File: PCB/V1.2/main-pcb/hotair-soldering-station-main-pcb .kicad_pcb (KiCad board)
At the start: 2 copper layers, 100 x 70 mm, 146 parts, among them J1 230VAC_IN, J10 T12_power (NS-25 r2,54), J11 LCD_CON2 (JST r.2.0), J12 LCD_CON1 (JST r.2.0), J13 ICP (goldpin r2,54), J14 Unused_GPIO, J2 FRONT_PANEL (IDC r. 2,54), J3 EARTH_GND, J4 24V_IN (NS-25 r2,54), J5 PSUPPLY (PWZ-02S r.3,96), J6 HOTAIR_FAN (JST r,2,54), J7 HOTAIR_MEAS (JST r.2,5), J8 HOTAIR_HEATER (PWZ-02S r.3,96), J9 WEP (r.2,54), Q1 BC817, Q10 RFP15P05, Q11 BC817, Q12 BC817, Q13 BC817, Q14 BC807, Q15 RFP15P05, Q2 BC807, Q3 BC817, Q4 RFP15P05, Q5 BC817, Q6 BT139-600, Q7 BC817, Q8 BC807, Q9 BC817, U1 MOC3041M, U2 MAX31855KASA, U3 MP1584-Step-Down, U4 AP1117-ADJ, U5 LM741, U6 AD8606, U8 STM32F103C6Tx

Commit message: Silkscreen progress
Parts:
- U3: value MP1584-Step-Down -> MP1584
- moved R9 2.41 mm to (72.0, 40.9)
- moved G*** 1.59 mm to (77.9, 45.3)
- moved D12 0.43 mm to (109.0, 48.6)
- moved C16 0.38 mm to (67.8, 46.6)
- moved C19 0.13 mm to (75.8, 67.3)
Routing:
- net THERM_GND: track 31.0 -> 33.2 mm
- net IRON_T12_TEMP_ADC: track 55.4 -> 53.3 mm
- net UART_DBG_TX: track 26.3 -> 25.3 mm
- net +3V3: track 214.1 -> 214.8 mm

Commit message: Front panel rocker switch connector change, preparing pcb for production
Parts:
- C13, C18, C19, C20, C6, C8: footprint Capacitors:0603 -> Capacitors:0805
- C9: footprint Capacitor_SMD:C_0603_1608Metric -> Capacitors:0805
- U3: value MP1584 -> MP1584-Step-Down
- moved C19 0.51 mm to (75.9, 67.8)
- moved C9 0.30 mm to (75.9, 66.1)
- moved C8 0.18 mm to (77.9, 54.8)
- moved C18 0.15 mm to (87.0, 56.5)
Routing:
- net +3V3: track 214.8 -> 215.6 mm

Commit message: Front panel done
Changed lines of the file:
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@@
       (effects (font (size 1 1) (thickness 0.15)) (justify mirror))
     )
+    (fp_line (start -2.5 2) (end 7.66 2) (layer "B.SilkS") (width 0.12))
     (fp_line (start 0.69 3.27) (end 0.7 2) (layer "B.SilkS") (width 0.12))
-    (fp_line (start -2.58 3.27) (end -2.58 -2.1) (layer "B.SilkS") (width 0.12))
-    (fp_line (start -2.58 3.27) (end 7.66 3.27) (layer "B.SilkS") (width 0.12))
     (fp_line (start -2.58 -2.1) (end 7.66 -2.1) (layer "B.SilkS") (width 0.12))
-    (fp_line (start -2.5 2) (end 7.66 2) (layer "B.SilkS") (width 0.12))
+    (fp_line (start -2.58 3.27) (end -2.58 -2.1) (layer "B.SilkS") (width 0.12))
     (fp_line (start 7.66 3.27) (end 7.66 -2.1) (layer "B.SilkS") (width 0.12))
     (fp_line (start 4.391 3.27) (end 4.391 2) (layer "B.SilkS") (width 0.12))
-    (fp_line (start 7.79 -1.51) (end 7.79 3.4) (layer "B.CrtYd") (width 0.05))
+    (fp_line (start -2.58 3.27) (end 7.66 3.27) (layer "B.SilkS") (width 0.12))
     (fp_line (start -2.71 3.4) (end -2.71 -1.51) (layer "B.CrtYd") (width 0.05))
-    (fp_line (start -2.71 -1.51) (end 7.79 -1.51) (layer "B.CrtYd") (width 0.05))
+    (fp_line (start 7.79 -1.51) (end 7.79 3.4) (layer "B.CrtYd") (width 0.05))
     (fp_line (start 7.79 3.4) (end -2.71 3.4) (layer "B.CrtYd") (width 0.05))
+    (fp_line (start -2.71 -1.51) (end 7.79 -1.51) (layer "B.CrtYd") (width 0.05))
     (fp_line (start 7.54 -2) (end 7.54 3.15) (layer "B.Fab") (width 0.1))
     (fp_line (start -2.46 2) (end 7.54 2) (layer "B.Fab") (width 0.1))
@@
   (gr_rect (start 58.547 50.292) (end 62.357 44.958) (layer "B.Cu") (width 0.2) (fill solid))
   (gr_rect (start 81.3444 18.6156) (end 85.6624 29.2836) (layer "B.Cu") (width 0.2) (fill solid))
+  (gr_circle (center 113.03 79.121) (end 109.641217 79.121) (layer "B.SilkS") (width 0.21) (fill solid))
+  (gr_circle (center 113.03 17.018) (end 109.641217 17.018) (layer "B.SilkS") (width 0.21) (fill solid))
+  (gr_circle (center 21.209 78.994) (end 17.820217 78.994) (layer "B.SilkS") (width 0.21) (fill solid))
   (gr_line (start 57.658 13.081) (end 57.658 82.804) (layer "B.SilkS") (width 0.4))
+  (gr_circle (center 21.082 17.018) (end 17.693217 17.018) (layer "B.SilkS") (width 0.21) (fill solid))
   (gr_line (start 50.8 82.804) (end 50.8 12.954) (layer "B.SilkS") (width 0.4))
   (gr_line (start 63.9064 55.372) (end 63.6524 55.372) (layer "F.SilkS") (width 0.21))
   (gr_line (start 57.658 82.804) (end 57.658 13.081) (layer "F.SilkS") (width 0.4))
+  (gr_circle (center 21.209 78.994) (end 24.597783 78.994) (layer "F.SilkS") (width 0.21) (fill solid))
+  (gr_circle (center 113.03 79.121) (end 116.418783 79.121) (layer "F.SilkS") (width 0.21) (fill solid))
+  (gr_circle (center 21.082 17.018) (end 24.470783 17.018) (layer "F.SilkS") (width 0.21) (fill solid))
   (gr_line (start 76.1492 46.2788) (end 75.8952 45.974) (layer "F.SilkS") (width 0.15))
   (gr_line (start 50.8 33.528) (end 50.8 13.081) (layer "F.SilkS") (width 0.4))
   (gr_line (start 80.01 46.2788) (end 76.454 46.2788) (layer "F.SilkS") (width 0.15))
+  (gr_circle (center 113.03 17.018) (end 116.418783 17.018) (layer "F.SilkS") (width 0.21) (fill solid))
   (gr_line (start 50.8 33.528) (end 50.8 82.804) (layer "F.SilkS") (width 0.4))
   (gr_line (start 76.454 46.2788) (end 76.1492 46.2788) (layer "F.SilkS") (width 0.15))

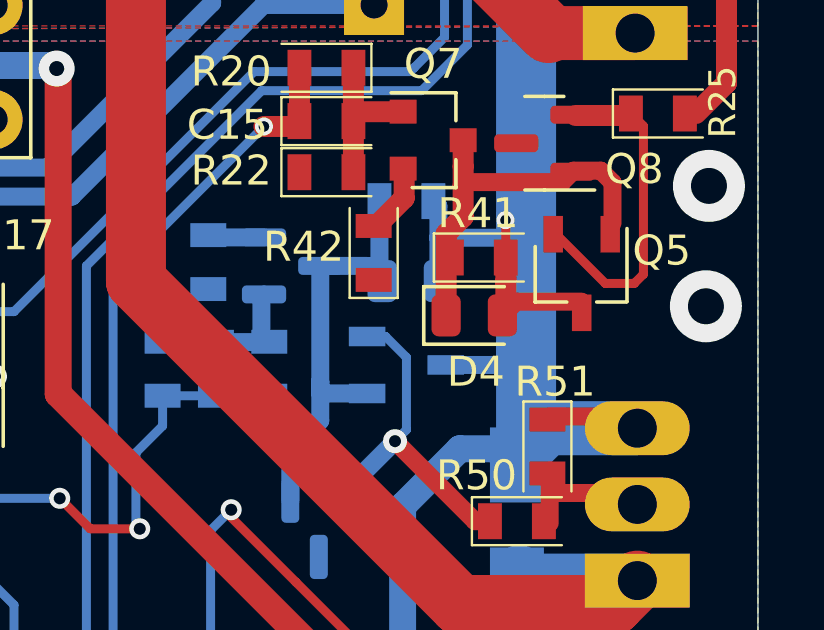
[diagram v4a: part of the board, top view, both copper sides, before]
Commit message: Zener diode footprint and orientation change
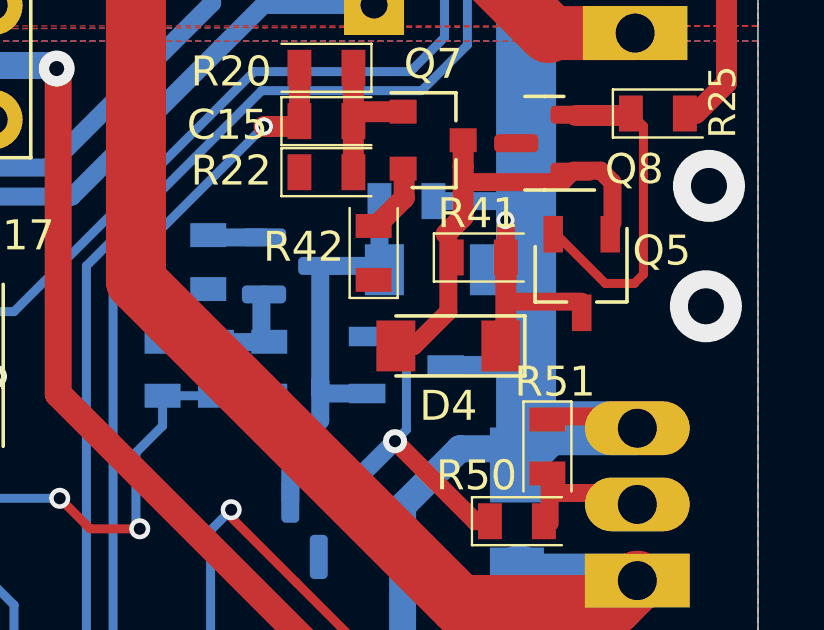
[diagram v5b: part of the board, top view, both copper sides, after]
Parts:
- D4, D9: footprint Diode_SMD:D_0805_2012Metric -> Diode_SMD:D_MiniMELF
- moved D4 1.33 mm to (106.7, 42.7), turned to 180 degrees
- moved D9 0.97 mm to (106.3, 40.1)
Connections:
- D4 pad 1: Net-(D4-Pad1) -> +24V
- D4 pad 2: +24V -> Net-(Q5-Pad1)
- Q5 pad 1: Net-(D4-Pad1) -> Net-(Q5-Pad1)
- Q7 pad 3: Net-(D4-Pad1) -> Net-(Q5-Pad1)
- Q8 pad 1: Net-(D4-Pad1) -> Net-(Q5-Pad1)
- R41 pad 1: Net-(D4-Pad1) -> Net-(Q5-Pad1)
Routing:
- net Net-(Q5-Pad1): track 0.00 -> 14.9 mm
- net Net-(D4-Pad1): track 12.8 -> 0.00 mm
- net +24V: track 144.2 -> 143.5 mm
